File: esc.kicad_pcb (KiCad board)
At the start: 6 copper layers, 40 x 45 mm, 196 parts, among them J1 Conn_01x02, J10 Conn_01x01_Pin, J11 Conn_01x01_Pin, J12 Conn_01x01_Pin, J13 Conn_01x01_Pin, J14 Conn_01x01_Pin, J15 Conn_01x01_Pin, J16 Conn_01x02, J17 Conn_01x01_Pin, J18 Conn_01x01_Pin, J19 Conn_01x01_Pin, J2 Conn_01x01_Pin, J20 Conn_01x01_Pin, J21 Conn_01x01_Pin, J22 Conn_01x01_Pin, J23 Conn_01x01_Pin, J25 Conn_01x01_Pin, J26 Conn_01x01_Pin, J27 Conn_01x01_Pin, J3 Conn_01x01_Pin, J4 Conn_01x01_Pin, J5 Conn_01x01_Pin, J6 Conn_01x01_Pin, J7 Conn_01x01_Pin, J8 Conn_01x01_Pin, J9 Conn_01x01_Pin, Q1 NP80N06D6, Q10 NP80N06D6, Q11 NP80N06D6, Q12 NP80N06D6, Q13 NP80N06D6, Q14 NP80N06D6, Q15 NP80N06D6, Q16 NP80N06D6, Q17 NP80N06D6, Q18 NP80N06D6, Q19 NP80N06D6, Q2 NP80N06D6, Q20 NP80N06D6, Q21 NP80N06D6, Q22 NP80N06D6, Q23 NP80N06D6, Q24 NP80N06D6, Q3 NP80N06D6, Q4 NP80N06D6, Q5 NP80N06D6, Q6 NP80N06D6, Q7 NP80N06D6, Q8 NP80N06D6, Q9 NP80N06D6, U2 STM32C011F6U6TR, U3 STDRIVE101, U4 STDRIVE101, U5 STM32C011F6U6TR, U6 STDRIVE101, U7 STM32C011F6U6TR, U8 STDRIVE101, U9 STM32C011F6U6TR

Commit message: ...
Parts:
- removed J16: Conn_01x02, deshan:Batt_Conn_HV
- added POWER_OUT1: Conn_01x02, deshan:Conn_01x01_power_x2, B.Cu at (230.0, 83.0)
- 3V3: renamed from J17; footprint deshan:Conn_1x1_small -> deshan:Conn_01x01_Pin
- POWER_IN1: renamed from J1; footprint deshan:Batt_Conn_HV -> deshan:Conn_01x01_power_x2
- moved C34 1.59 mm to (232.2, 59.9), turned to 0 degrees
- moved C49 1.57 mm to (228.2, 60.8), turned to 0 degrees
- moved C4 1.51 mm to (228.5, 59.8), turned to 0 degrees
- moved R19 1.03 mm to (226.6, 77.7)
- moved C36 0.96 mm to (235.2, 58.4)
- moved R38 0.94 mm to (230.4, 57.9)
- moved R39 0.94 mm to (230.4, 58.9)
- moved C16 0.91 mm to (227.6, 77.7)
- moved C3 0.86 mm to (231.1, 41.6)
- moved C35 0.84 mm to (233.7, 58.4)
- moved R1 0.78 mm to (233.5, 42.2)
- moved C2 0.78 mm to (231.1, 42.7)
- moved C1 0.78 mm to (232.5, 42.2)
- moved C31 0.78 mm to (227.4, 42.2)
- moved R37 0.76 mm to (226.4, 42.2)
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- renumbered J2 to DShot_M1, J18 to DShot_M2, J19 to DShot_M3, J20 to DShot_M4, J4 to J1, J13 to J10, J14 to J11, J15 to J12, J5 to J2, J6 to J3, J7 to J4, J8 to J5, J9 to J6, J10 to J7, J11 to J8, J12 to J9, J21 to SWCLK_M1, J23 to SWCLK_M2, J26 to SWCLK_M3, J27 to SWCLK_M4, J3 to SWDIO_M1, J22 to SWDIO_M2, J24 to SWDIO_M3, J25 to SWDIO_M4
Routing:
- net GND: track 26.3 -> 39.5 mm, vias 124 -> 148
- net OUT2: track 99.3 -> 107.1 mm
- net B+: track 33.4 -> 39.0 mm, vias 102 -> 106
- net 3V3: track 16.9 -> 14.3 mm, vias 11 -> 12
- net SWDIO_M3: track 16.6 -> 14.0 mm
- net SWCLK_M3: track 13.6 -> 11.6 mm
- net Net-(U8-REG12): track 8.72 -> 10.7 mm
- net PHASE_A_M1: track 1.59 -> 3.50 mm
- net Net-(Q19-G): track 0.00 -> 1.80 mm
- net Net-(Q3-G): track 0.00 -> 1.80 mm
- net Net-(Q1-G): track 0.00 -> 1.80 mm
- net SWDIO_M1: track 16.4 -> 14.7 mm
- net Net-(Q21-G): track 0.00 -> 1.73 mm
- net Net-(Q7-G): track 0.00 -> 1.66 mm
- net Net-(Q23-G): track 0.00 -> 1.65 mm
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- added copper zone on B.Cu, net OUT1
- added copper zone on F.Cu, net OUT1
- added copper zone on B.Cu, net OUT2
- added copper zone on F.Cu, net OUT2
- added copper zone on B.Cu, net OUT3
- added copper zone on F.Cu, net OUT3

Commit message: ...
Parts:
- moved C19 3.90 mm to (233.7, 62.3), turned to 90 degrees
- moved R20 3.53 mm to (232.7, 62.3), turned to -90 degrees
- moved C20 3.23 mm to (234.9, 62.3)
- moved C21 3.23 mm to (236.3, 62.3)
- moved R23 2.70 mm to (230.5, 62.3)
- moved C4 2.69 mm to (226.3, 58.3), turned to -90 degrees
- moved R22 2.64 mm to (229.5, 62.3)
- moved R21 2.53 mm to (231.7, 62.3), turned to 90 degrees
- moved C49 2.46 mm to (226.3, 62.3), turned to 90 degrees
- moved R38 2.29 mm to (232.7, 58.3), turned to 90 degrees
- moved R2 2.24 mm to (227.3, 58.3), turned to 90 degrees
- moved C34 2.19 mm to (233.7, 58.3), turned to -90 degrees
- moved C6 2.04 mm to (223.7, 58.3)
- moved C5 1.92 mm to (225.1, 58.3)
- moved R56 1.90 mm to (227.3, 62.3), turned to -90 degrees
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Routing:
- net OUT1: track 155.0 -> 162.1 mm
- net B+: track 39.0 -> 33.7 mm
- net GND: track 39.5 -> 34.6 mm
- net GLS1: track 42.6 -> 45.8 mm
- net OUT2: track 107.1 -> 104.1 mm
- net Net-(U6-REG12): track 8.88 -> 11.1 mm
- net GHS1: track 73.9 -> 75.9 mm
- net Net-(U4-REG12): track 8.89 -> 10.6 mm
- net Net-(U6-DT/MODE): track 7.37 -> 6.12 mm
- net Net-(U6-CP): track 6.45 -> 5.23 mm
- net Net-(U3-REG12): track 9.90 -> 10.7 mm
- net Net-(U8-DT/MODE): track 6.94 -> 6.22 mm
- net Net-(U8-CP): track 6.27 -> 5.58 mm
- net Net-(U3-DT/MODE): track 7.00 -> 6.33 mm
- net Net-(U3-CP): track 5.98 -> 5.33 mm
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
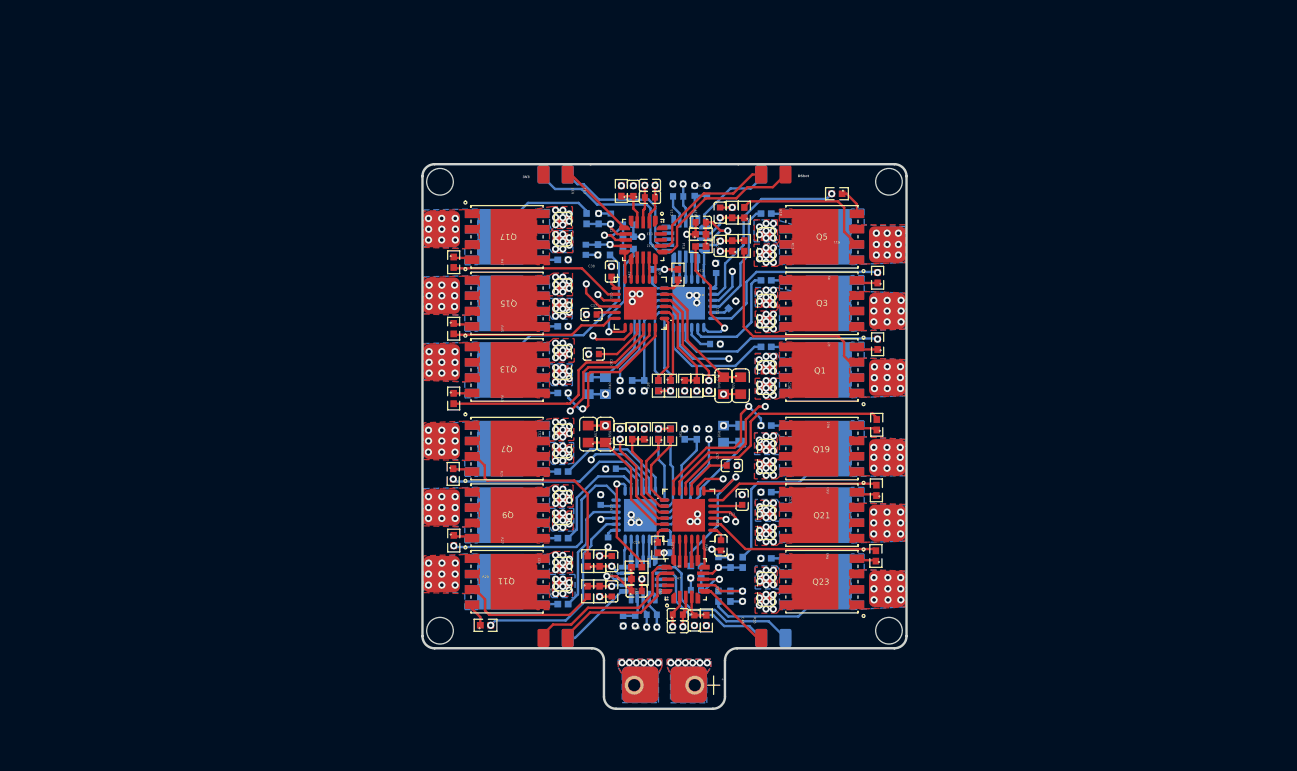
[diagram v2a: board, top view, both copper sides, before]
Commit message: change in architecture with horizonatal half bridge
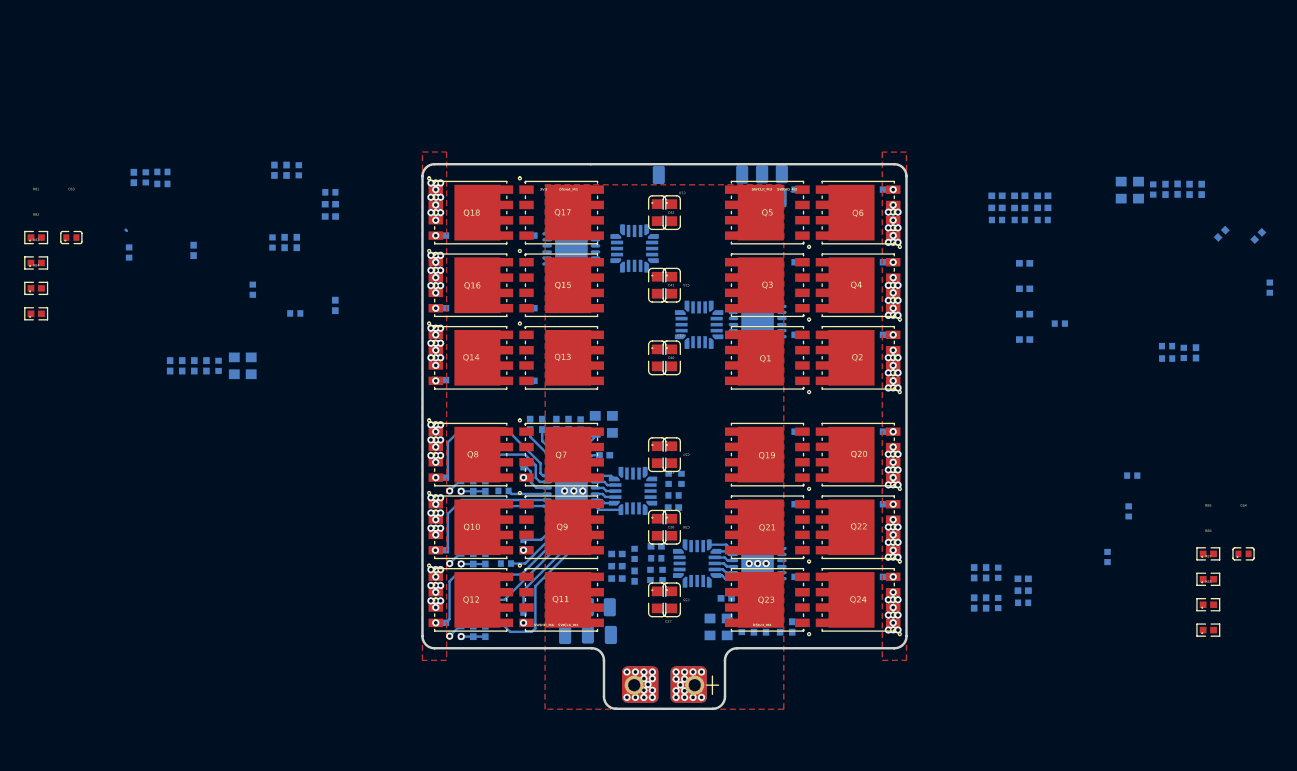
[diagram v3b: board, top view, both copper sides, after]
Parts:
- removed REF** (x4): MountingHole_2.2mm_M2, MountingHole:MountingHole_2.2mm_M2
- removed U2: STM32C011F6U6TR, easyeda2kicad:UFQFPN-20_L3.0-W3.0-P0.50-TL
- added C61: 4.7nF, easyeda2kicad:C0402, B.Cu at (262.7, 53.2)
- added C62: 4.7nF, easyeda2kicad:C0402, B.Cu at (227.5, 72.2)
- added C63: 4.7nF, easyeda2kicad:C0402, F.Cu at (181.0, 46.1)
- added C64: 4.7nF, easyeda2kicad:C0402, F.Cu at (277.9, 72.2)
- added M1: STM32C011F6U6TR, easyeda2kicad:UFQFPN-20_L3.0-W3.0-P0.50-TL, B.Cu at (232.9, 53.3)
- added R73: 100k, easyeda2kicad:R0402, B.Cu at (259.8, 48.2)
- added R74: 100k, easyeda2kicad:R0402, B.Cu at (259.8, 50.3)
- added R75: 100k, easyeda2kicad:R0402, B.Cu at (259.8, 52.4)
- added R76: 10k, easyeda2kicad:R0402, B.Cu at (259.8, 54.5)
- added R77: 100k, easyeda2kicad:R0402, B.Cu at (226.1, 72.2)
- added R78: 10k, easyeda2kicad:R0402, B.Cu at (227.5, 74.0)
- added R79: 100k, easyeda2kicad:R0402, B.Cu at (226.1, 73.2)
- added R80: 100k, easyeda2kicad:R0402, B.Cu at (226.1, 74.2)
- added R81: 100k, easyeda2kicad:R0402, F.Cu at (178.1, 46.1)
- added R82: 10k, easyeda2kicad:R0402, F.Cu at (178.1, 48.2)
- added R83: 100k, easyeda2kicad:R0402, F.Cu at (178.1, 50.3)
- added R84: 100k, easyeda2kicad:R0402, F.Cu at (178.1, 52.4)
- added R85: 100k, easyeda2kicad:R0402, F.Cu at (274.9, 72.2)
- added R86: 10k, easyeda2kicad:R0402, F.Cu at (274.9, 74.3)
- added R87: 100k, easyeda2kicad:R0402, F.Cu at (274.9, 76.4)
- added R88: 100k, easyeda2kicad:R0402, F.Cu at (274.9, 78.5)
- 3V3, C13, C14, C15, C28, C29, C30, C31, C32, C33, C34, C35, C36, C37, C38, C39, C46, C47, C48, C49, C50, C51, C52, C53, C54, DShot_M3, DShot_M4, J1, J10, J11, J12, J2, J3, J4, J5, J6, J7, J8, J9, R11, R13, R14, R15, R16, R17, R18, R25, R27, R29, R31, R32, R33, R34, R35, R36, R37, R38, R39, R40, R41, R42, R43, R45, R47, R55, R56, R57, R58, R59, R60, R61, R63, R65, R7, R9, SWCLK_M3, SWCLK_M4, SWDIO_M3, SWDIO_M4: moved to B.Cu
- GD3: renamed from U8; moved to B.Cu
- GD4: renamed from U4; moved to B.Cu
- M3: renamed from U9; moved to B.Cu
- M4: renamed from U5; moved to B.Cu
- Q10, Q12, Q14, Q16, Q18, Q2, Q20, Q22, Q24, Q4, Q6, Q8: moved to F.Cu
- moved R3 47.0 mm to (272.4, 42.1), turned to 90 degrees
- moved R2 47.0 mm to (271.4, 42.1), turned to -90 degrees
- moved C4 46.9 mm to (270.4, 42.1), turned to 90 degrees
- moved C5 46.9 mm to (269.2, 42.1), turned to 90 degrees
- moved C6 46.9 mm to (267.7, 42.1), turned to 90 degrees
- moved R4 46.8 mm to (274.4, 42.1), turned to -90 degrees
- moved R5 46.8 mm to (273.4, 42.1), turned to 90 degrees
- moved C7 46.1 mm to (280.0, 50.2), turned to 90 degrees
- moved C8 43.8 mm to (279.1, 45.9)
- moved C1 42.6 mm to (272.9, 55.6)
- moved C2 42.6 mm to (271.5, 56.1)
- moved R1 42.6 mm to (273.9, 55.6)
- moved C3 42.6 mm to (271.5, 55.0)
- moved C9 41.9 mm to (276.1, 45.8), turned to -135 degrees
- moved C34 40.6 mm to (193.2, 56.7)
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- renumbered U3 to GD1, U6 to GD2, U7 to M2
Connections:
- M2 pad 5: unconnected-(U7-PA0-Pad5) -> VIRTUAL_NEUTRAL_POINT
- M3 pad 5: unconnected-(U9-PA0-Pad5) -> VIRTUAL_NEUTRAL_POINT
- M4 pad 5: unconnected-(U5-PA0-Pad5) -> VIRTUAL_NEUTRAL_POINT
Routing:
- net OUT1: track 162.1 -> 9.66 mm, vias 44 -> 0
- net OUT2: track 104.1 -> 8.85 mm, vias 44 -> 0
- net OUT3: track 120.0 -> 29.4 mm, vias 44 -> 0
- net GHS1: track 75.9 -> 3.17 mm, vias 2 -> 0
- net GHS2: track 62.9 -> 4.01 mm, vias 2 -> 0
- net GHS3: track 61.0 -> 9.99 mm, vias 2 -> 0
- net GLS1: track 45.8 -> 13.7 mm, vias 4 -> 0
- net B+: track 33.7 -> 3.30 mm, vias 106 -> 13
- net GND: track 34.6 -> 6.87 mm, vias 148 -> 166
- net GLS2: track 33.0 -> 11.8 mm, vias 4 -> 0
- net GLS3: track 33.6 -> 16.2 mm, vias 4 -> 0
- net SWDIO_M1: track 14.7 -> 0.00 mm
- net 3V3: track 14.3 -> 0.00 mm, vias 14 -> 0
- net SWDIO_M3: track 14.0 -> 0.00 mm
- net SWDIO_M2: track 13.9 -> 0.00 mm
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- added copper zone on In1.Cu, net GND
- removed copper zone on In4.Cu, net 3V3
- removed copper zone on B.Cu, net B+
- removed copper zone on In1.Cu, net B+
- removed copper zone on B.Cu, net GND
- removed copper zone on In2.Cu, net GND
- removed copper zone on B.Cu, net OUT1
- removed copper zone on F.Cu, net OUT1
- removed copper zone on B.Cu, net OUT2
- removed copper zone on F.Cu, net OUT2
- removed copper zone on B.Cu, net OUT3
- removed copper zone on F.Cu, net OUT3
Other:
- copper layers 6 -> 4
- board text added: "DShot_M1"
- board text added: "DShot_M2"
- board text added: "DShot_M3"
- board text added: "DShot_M4"
- board text added: "SWCLK_M1"
- board text added: "SWCLK_M2"
- board text added: "SWCLK_M3"
- board text added: "SWCLK_M4"
- board text added: "SWDIO_M1"
- board text added: "SWDIO_M2"
- board text added: "SWDIO_M3"
- board text added: "SWDIO_M4"
- board text removed: "DShot"

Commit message: ...
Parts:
- R2, R20, R38, R56: value 18k -> 100k
- R21, R3, R39, R57: value 10k -> 18k
- SWCLK_M1, SWCLK_M2, SWCLK_M3, SWCLK_M4, SWDIO_M1, SWDIO_M2, SWDIO_M4: moved to F.Cu
- SWDIO_M3: value ~ -> Conn_01x01_Pin; moved to F.Cu
- moved SWDIO_M4 50.5 mm to (234.5, 29.2), turned to 0 degrees
- moved SWCLK_M4 50.5 mm to (232.5, 29.2), turned to 0 degrees
- moved SWDIO_M2 43.9 mm to (234.5, 33.7), turned to 0 degrees
- moved SWCLK_M2 43.8 mm to (232.5, 33.7), turned to 0 degrees
- moved SWCLK_M3 16.4 mm to (226.5, 29.2), turned to 0 degrees
- moved SWDIO_M3 16.2 mm to (228.5, 29.2), turned to 0 degrees
- moved SWCLK_M1 14.8 mm to (226.5, 33.7), turned to 0 degrees
- moved SWDIO_M1 12.2 mm to (228.5, 33.7), turned to 0 degrees
